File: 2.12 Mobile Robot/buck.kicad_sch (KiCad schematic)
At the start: 17 parts, among them SW4 SW_PWR, U4 POWER_IN, U5 TPS564208DDCT

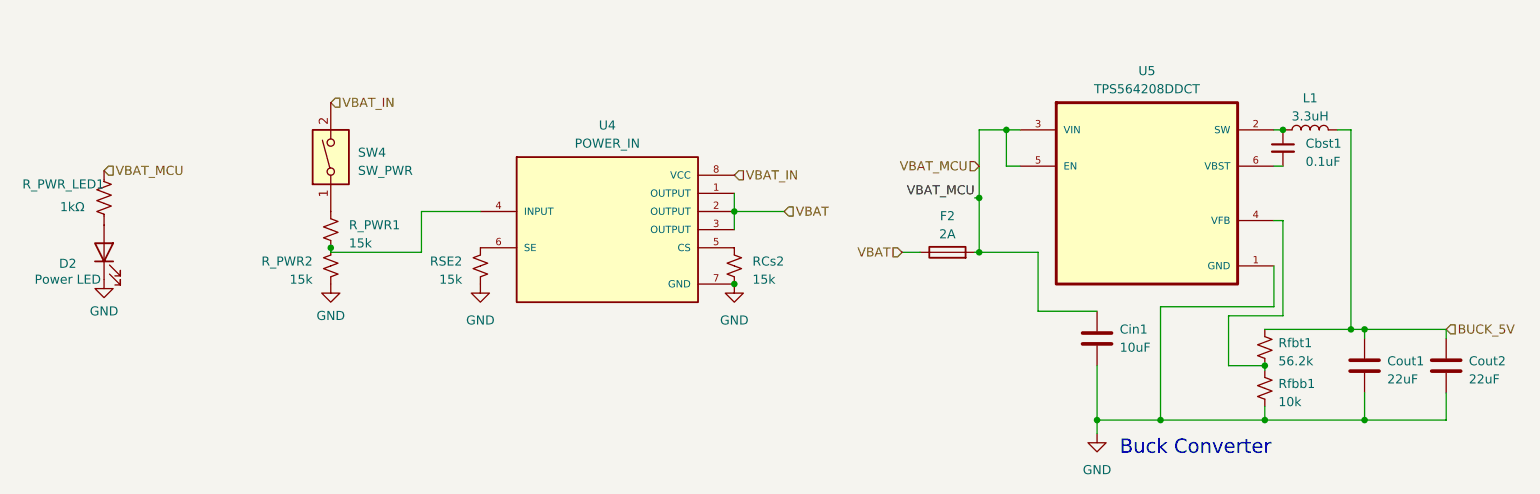
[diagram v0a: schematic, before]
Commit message: Passed DRC
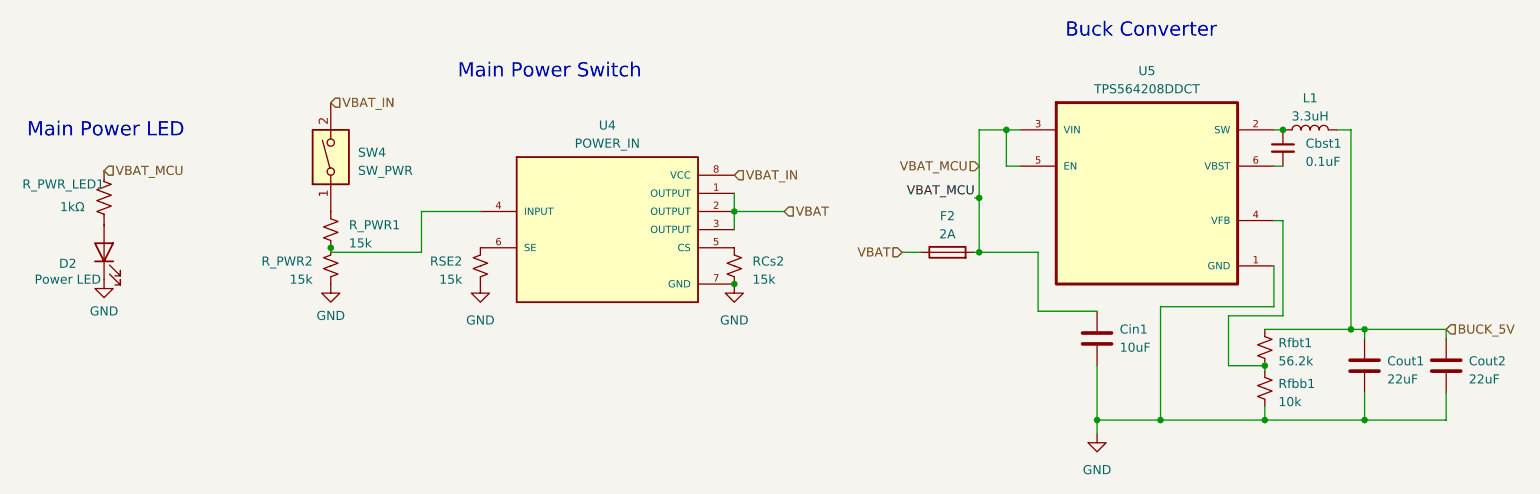
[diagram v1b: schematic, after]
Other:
- note added: "Main Power LED"
- note added: "Main Power Switch"
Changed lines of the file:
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@@
     (stroke (width 0) (type default))
   )
-  (text "Buck Converter" (at 189.865 126.365 0)
+  (text "Main Power Switch" (at 97.155 73.66 0)
     (effects (font (size 2 2)) (justify left bottom))
   )
+  (text "Main Power LED" (at 36.83 81.915 0)
+    (effects (font (size 2 2)) (justify left bottom))
+  )
+  (text "Buck Converter" (at 182.245 67.945 0)
+    (effects (font (size 2 2)) (justify left bottom))
+  )

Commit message: Changed some of the footprints
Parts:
- SW4: footprint Connector_JST:JST_PH_B2B-PH-SM4-TB_1x02-1MP_P2.00mm_Vertical -> 2.679:SW_500SSP1S1M6QEA; MPN C160352 -> (none)
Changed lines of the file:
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@@
       (effects (font (size 1.27 1.27)) (justify right))
     )
-    (property "Footprint" "Connector_JST:JST_PH_B2B-PH-SM4-TB_1x02-1MP_P2.00mm_Vertical" (at 79.375 84.455 0)
+    (property "Footprint" "2.679:SW_500SSP1S1M6QEA" (at 79.375 84.455 0)
       (effects (font (size 1.27 1.27)) hide)
     )
-    (property "Datasheet" "~" (at 79.375 84.455 0)
+    (property "Datasheet" "https://www.digikey.com/en/products/detail/e-switch/500SSP1S1M6QEA/378947" (at 79.375 84.455 0)
       (effects (font (size 1.27 1.27)) hide)
     )
-    (property "MPN" "C160352" (at 79.375 84.455 90)
-      (effects (font (size 1.27 1.27)) hide)
-    )
